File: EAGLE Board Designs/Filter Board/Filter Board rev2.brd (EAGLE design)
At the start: 50.8 x 152.4 mm, 102 parts, among them J4 CONNECTOR-40__, J5 CONNECTOR-40__, U10 MAX7400, U11 MAX7400, U19 MAX7400, U20 MAX7400, U21 MAX7400, U22 MAX7400, U23 MAX7400, U24 MAX7400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

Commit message: fixed drc
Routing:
- net GND: track 59.9 -> 62.7 mm, vias 11 -> 10
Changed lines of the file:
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@@
 <wire x1="44.4956" y1="63.4844" x2="45.45" y2="62.53" width="0.254" layer="16"/>
 <via x="20.574" y="41.402" extent="1-16" drill="0.3556"/>
-<via x="24.13" y="41.402" extent="1-16" drill="0.3556"/>
 <wire x1="19.292" y1="35.052" x2="20.574" y2="35.052" width="0.254" layer="1"/>
 <via x="20.574" y="35.052" extent="1-16" drill="0.3556"/>
@@
 <contactref element="C6" pad="2"/>
 <contactref element="C2" pad="2"/>
-<wire x1="20.574" y1="41.402" x2="24.13" y2="41.402" width="0.254" layer="16"/>
 <wire x1="19.292" y1="41.402" x2="20.574" y2="41.402" width="0.254" layer="1"/>
 <wire x1="19.546" y1="68.326" x2="21.082" y2="68.326" width="0.254" layer="1"/>
@@
 <wire x1="19.292" y1="44.196" x2="19.292" y2="41.402" width="0.254" layer="1"/>
 <wire x1="19.292" y1="35.052" x2="19.292" y2="32.258" width="0.254" layer="1"/>
+<wire x1="20.574" y1="41.402" x2="20.574" y2="35.052" width="0.254" layer="16"/>
 </signal>
 <signal name="LOAD_FL_EXT">
@@
 <contactref element="J4" pad="17"/>
 <contactref element="U7" pad="5"/>
-<wire x1="43.45" y1="105.87" x2="43.386" y2="105.87" width="0.254" layer="1"/>
 <wire x1="43.45" y1="105.87" x2="41.212" y2="103.632" width="0.254" layer="1"/>
 <wire x1="41.212" y1="103.632" x2="29.464" y2="103.632" width="0.254" layer="1"/>
@@
 <signal name="SPN_POT_2">
 <contactref element="J4" pad="25"/>
-<wire x1="43.116" y1="97.536" x2="43.45" y2="97.87" width="0.254" layer="1"/>
 <contactref element="R4" pad="2"/>
 <contactref element="R6" pad="1"/>
@@
 <wire x1="30.734" y1="95.9224" x2="30.834" y2="95.8224" width="0.254" layer="1"/>
 <wire x1="34.798" y1="95.8224" x2="33.02" y2="95.8224" width="0.254" layer="1"/>
-<wire x1="43.45" y1="97.87" x2="41.4024" y2="95.8224" width="0.254" layer="1"/>
-<wire x1="41.4024" y1="95.8224" x2="34.798" y2="95.8224" width="0.254" layer="1"/>
+<wire x1="34.798" y1="95.8224" x2="41.4024" y2="95.8224" width="0.254" layer="1"/>
+<wire x1="41.4024" y1="95.8224" x2="43.45" y2="97.87" width="0.254" layer="1"/>
 </signal>
 <signal name="SPN_POT_3">
@@
 <wire x1="33.02" y1="86.9832" x2="30.834" y2="86.9832" width="0.254" layer="1"/>
 <wire x1="34.798" y1="86.9832" x2="33.02" y2="86.9832" width="0.254" layer="1"/>
-<wire x1="34.798" y1="86.9832" x2="34.886" y2="87.0712" width="0.254" layer="1"/>
 <wire x1="43.45" y1="89.87" x2="43.45" y2="89.844" width="0.254" layer="1"/>
 <wire x1="43.45" y1="89.844" x2="40.5892" y2="86.9832" width="0.254" layer="1"/>
@@
 <contactref element="C2" pad="1"/>
 <wire x1="45.45" y1="40.53" x2="45.068" y2="40.53" width="0.254" layer="1"/>
-<wire x1="44.2764" y1="41.3216" x2="37.4236" y2="41.3216" width="0.254" layer="1"/>
-<wire x1="37.4236" y1="41.3216" x2="37.338" y2="41.236" width="0.254" layer="1"/>
-<wire x1="45.068" y1="40.53" x2="44.2764" y2="41.3216" width="0.254" layer="1"/>
+<wire x1="44.0224" y1="41.5756" x2="37.6776" y2="41.5756" width="0.254" layer="1"/>
+<wire x1="37.6776" y1="41.5756" x2="37.338" y2="41.236" width="0.254" layer="1"/>
+<wire x1="45.068" y1="40.53" x2="44.0224" y2="41.5756" width="0.254" layer="1"/>
 <wire x1="37.338" y1="41.236" x2="34.898" y2="41.236" width="0.254" layer="1"/>
 <wire x1="34.798" y1="41.136" x2="34.898" y2="41.236" width="0.254" layer="1"/>
@@
 <wire x1="5.08" y1="30.492" x2="7.62" y2="30.492" width="0.254" layer="1"/>
 <wire x1="23.876" y1="29.222" x2="26.416" y2="29.222" width="0.254" layer="1"/>
-<wire x1="5.334" y1="40.144" x2="7.62" y2="40.144" width="0.254" layer="1"/>
-<wire x1="7.62" y1="40.144" x2="7.759" y2="40.259" width="0.254" layer="1"/>
-<wire x1="7.759" y1="40.259" x2="10.0965" y2="40.259" width="0.254" layer="1"/>
-<wire x1="5.334" y1="49.034" x2="7.62" y2="49.034" width="0.254" layer="1"/>
-<wire x1="7.62" y1="49.034" x2="7.759" y2="49.149" width="0.254" layer="1"/>
-<wire x1="7.759" y1="49.149" x2="10.0965" y2="49.149" width="0.254" layer="1"/>
 <wire x1="7.62" y1="58.178" x2="5.08" y2="58.178" width="0.254" layer="1"/>
-<wire x1="7.759" y1="58.039" x2="10.0965" y2="58.039" width="0.254" layer="1"/>
 <wire x1="24.13" y1="51.066" x2="26.67" y2="51.066" width="0.254" layer="1"/>
 <wire x1="26.67" y1="51.066" x2="26.555" y2="51.181" width="0.254" layer="1"/>
@@
 <wire x1="9.4735" y1="30.492" x2="10.0965" y2="31.115" width="0.254" layer="1"/>
 <wire x1="24.384" y1="61.734" x2="26.67" y2="61.734" width="0.254" layer="1"/>
-<wire x1="7.759" y1="58.039" x2="7.62" y2="58.178" width="0" layer="19" extent="1-1"/>
+<wire x1="5.334" y1="40.144" x2="7.62" y2="40.144" width="0.254" layer="1"/>
+<wire x1="7.62" y1="40.144" x2="9.9815" y2="40.144" width="0.254" layer="1"/>
+<wire x1="9.9815" y1="40.144" x2="10.0965" y2="40.259" width="0.254" layer="1"/>
+<wire x1="5.334" y1="49.034" x2="7.62" y2="49.034" width="0.254" layer="1"/>
+<wire x1="7.62" y1="49.034" x2="9.9815" y2="49.034" width="0.254" layer="1"/>
+<wire x1="9.9815" y1="49.034" x2="10.0965" y2="49.149" width="0.254" layer="1"/>
+<wire x1="10.0965" y1="58.039" x2="7.759" y2="58.039" width="0.254" layer="1"/>
+<wire x1="7.759" y1="58.039" x2="7.62" y2="58.178" width="0.254" layer="1"/>
 </signal>
 <signal name="CURRENT">

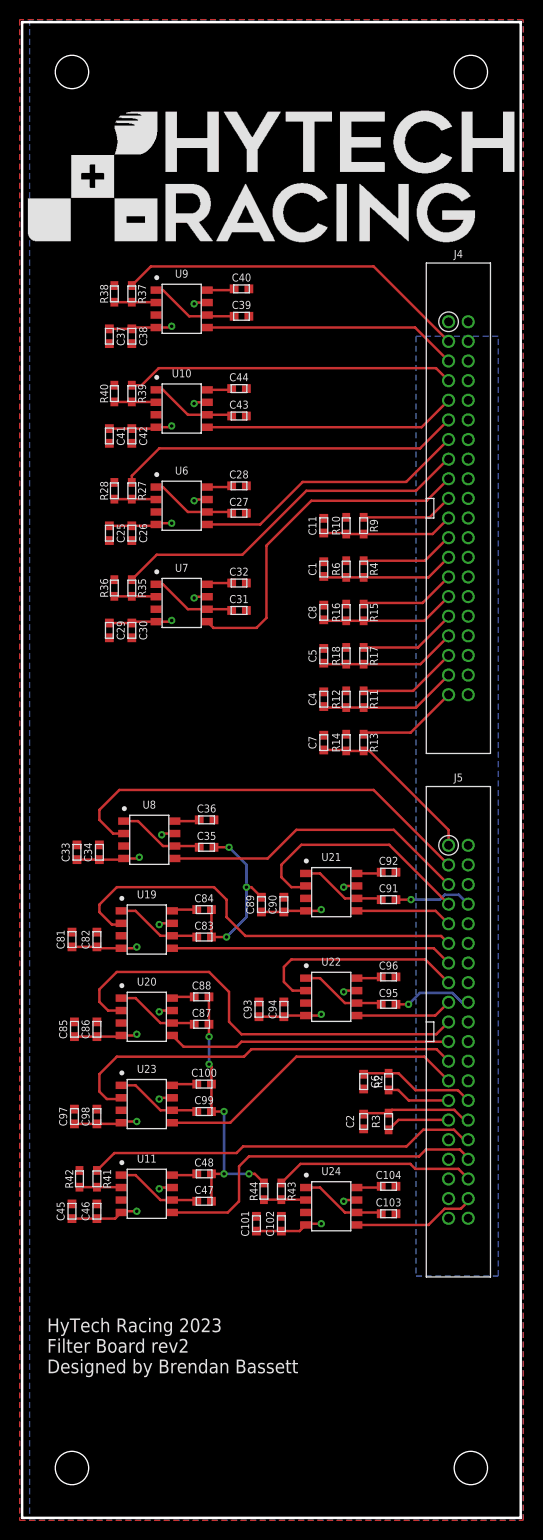
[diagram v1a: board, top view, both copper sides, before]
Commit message: updated passive filters and routing
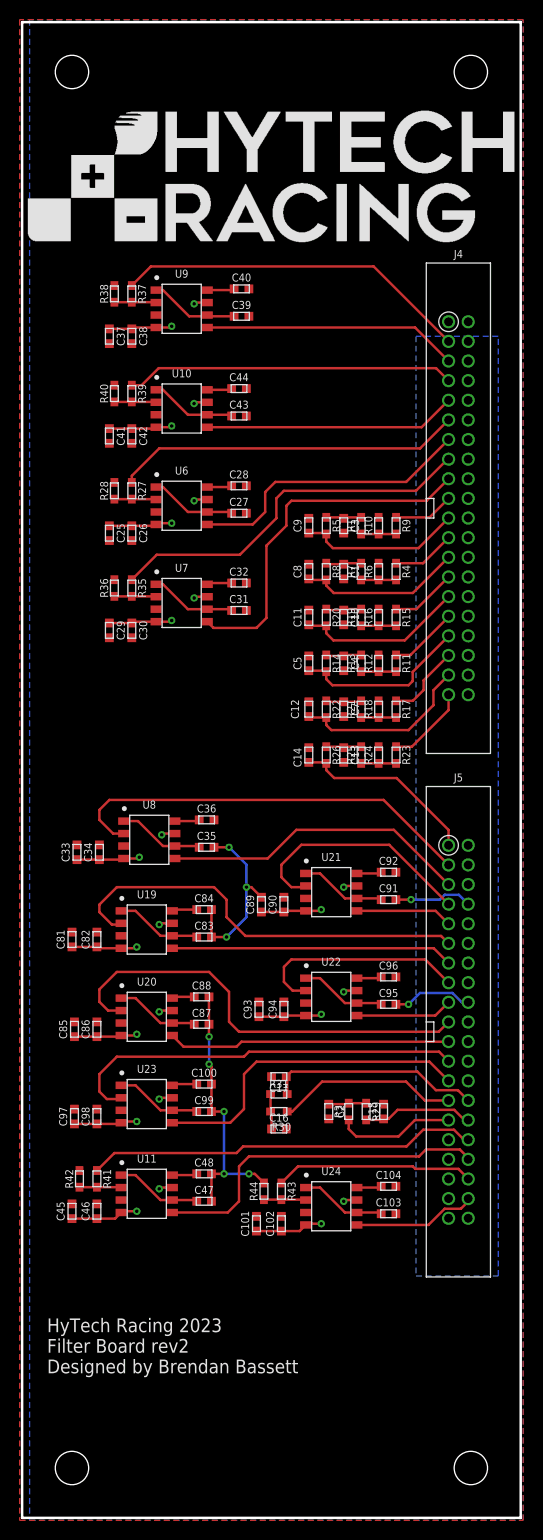
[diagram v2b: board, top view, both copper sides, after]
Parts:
- removed C6: CAPACITOR_0603_25V_1UF, HyTechDevices:0603-CAP
- removed R2: RESISTOR_0603_3.3K, HyTechDevices:0603-RES
- added C10, C12, C13, C14, C15, C16, C17, C3, C9: CAPACITOR_0603_10V_68NF, HyTechDevices:0603-CAP
- added R1, R19, R20, R21, R22, R25, R26, R29, R30, R31, R5, R7, R8: RESISTOR_0603_10K, HyTechDevices:0603-RES
- added R23: RESISTOR_0603_13K, HyTechDevices:0603-RES
- added R24: RESISTOR_0603_3.3K, HyTechDevices:0603-RES
- C1, C11, C2, C4, C5, C7, C8: value CAPACITOR_0603_25V_1UF -> CAPACITOR_0603_10V_68NF
- R13: value RESISTOR_0603_13K -> RESISTOR_0603_10K
- R14, R3: value RESISTOR_0603_3.3K -> RESISTOR_0603_10K
- moved C11 9.47 mm to (29.2, 91.7)
- moved R14 8.33 mm to (31.0, 87.1), turned to 270 degrees
- moved R13 8.08 mm to (34.5, 87.1), turned to 90 degrees
- moved R17 6.36 mm to (38.1, 82.4)
- moved R18 6.36 mm to (36.3, 82.4)
- moved R11 4.93 mm to (38.1, 87.1)
- moved R12 4.93 mm to (36.3, 87.1)
- moved C8 4.44 mm to (29.2, 96.4)
- moved R3 4.19 mm to (33.3, 41.4)
- moved C4 4.18 mm to (32.8, 87.1), turned to 270 degrees
- moved C7 3.96 mm to (32.8, 82.4), turned to 270 degrees
- moved C2 3.70 mm to (31.2, 41.4)
- moved R15 3.34 mm to (38.1, 91.7)
- moved R16 3.34 mm to (36.3, 91.7)
- moved R4 3.31 mm to (38.1, 96.4)
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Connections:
- new net N$10: R11.2, R12.1, R13.1
- new net N$11: C7.1, R21.2, R22.1
- new net N$12: R17.2, R18.1, R21.1
- new net N$25: C13.1, R25.2, R26.1
- new net N$26: R23.2, R24.1, R25.1
- new net N$27: C2.1, R29.1, R3.2
- new net N$28: C16.1, R30.2, R31.1
- new net N$3: C3.1, R1.2, R5.1
- new net N$4: C1.1, R7.2, R8.1
- new net N$5: R1.1, R10.1, R9.2
- new net N$6: R4.2, R6.1, R7.1
- new net N$7: C10.1, R19.2, R20.1
- new net N$8: R15.2, R16.1, R19.1
- new net N$9: C4.1, R13.2, R14.1
- net BRAKE_PRESSURE_F: now also C17.1, R31.2; no longer C6.1, R2.2
- net BRAKE_PRESSURE_F_EXT: now also R30.1; no longer R2.1
- net BRAKE_PRESSURE_R: now also C15.1, R29.2; no longer C2.1, R3.2
- net GND: now also C10.2, C12.2, C13.2, C14.2, C15.2, C16.2, C17.2, C3.2, C9.2, R24.2; no longer C6.2, R14.2
- net SPN_POT_1: now also C9.1, R5.2; no longer C11.1, R10.1, R9.2
- net SPN_POT_2: now also C8.1, R8.2; no longer C1.1, R4.2, R6.1
- net SPN_POT_3: now also C11.1, R20.2; no longer C8.1, R15.2, R16.1
- net SPN_POT_4: now also R14.2; no longer R17.2, R18.1
- net SPN_POT_4_EXT: now also R11.1; no longer R17.1
- net SPN_POT_5: now also C12.1, R22.2; no longer C4.1, R11.2, R12.1
- net SPN_POT_5_EXT: now also R17.1; no longer R11.1
- net SPN_POT_6: now also C14.1, R26.2; no longer C7.1, R13.2, R14.1
- net SPN_POT_6_EXT: now also R23.1; no longer R13.1
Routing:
- net BRAKE_PRESSURE_F_EXT: track 6.56 -> 18.5 mm
- net BRAKE_PRESSURE_F: track 11.8 -> 21.8 mm
- net BRAKE_PRESSURE_R_EXT: track 6.54 -> 12.1 mm
- net SPN_POT_5: track 14.1 -> 18.5 mm
- net SPN_POT_4: track 14.0 -> 17.9 mm
- net N$27: track 0.00 -> 3.85 mm
- net N$11: track 0.00 -> 3.64 mm
- net N$7: track 0.00 -> 3.64 mm
- net N$9: track 0.00 -> 3.64 mm
- net N$4: track 0.00 -> 3.64 mm
- net N$3: track 0.00 -> 3.64 mm
- net N$25: track 0.00 -> 3.64 mm
- net N$28: track 0.00 -> 3.60 mm
- net N$8: track 0.00 -> 3.56 mm
- net N$6: track 0.00 -> 3.56 mm
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
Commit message: labels for all passive components visible
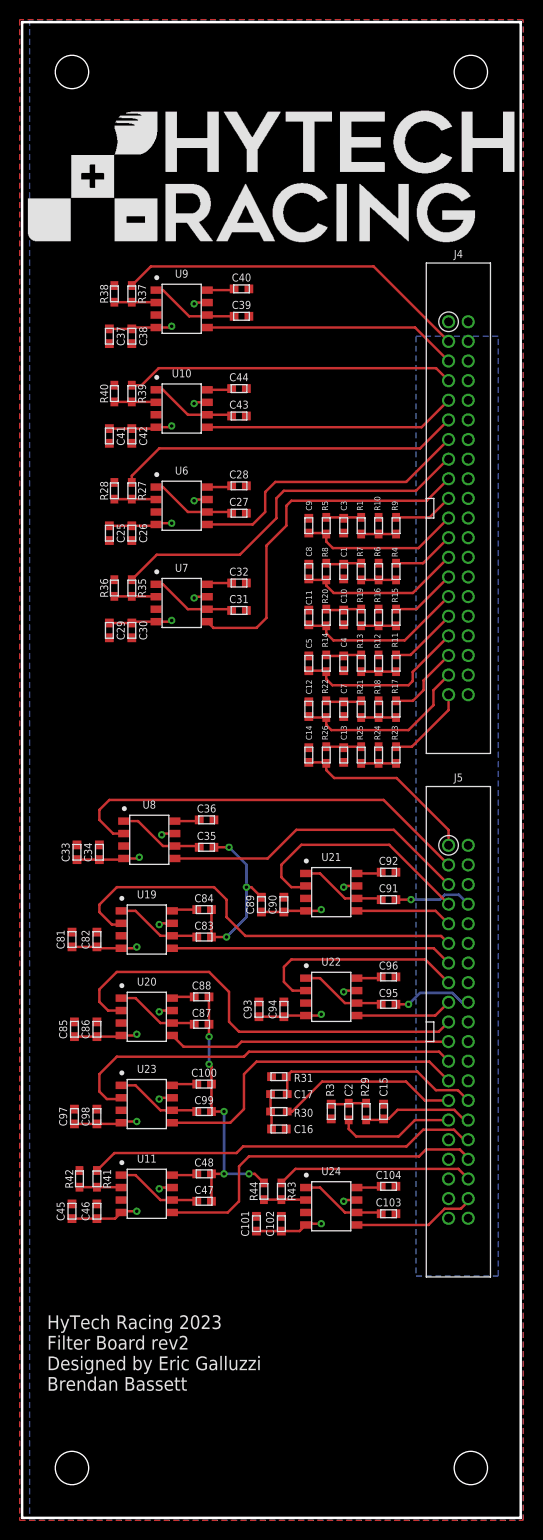
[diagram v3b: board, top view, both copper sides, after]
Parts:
- moved C2 0.25 mm to (31.5, 41.4)
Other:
- board text added: "HyTech Racing 2023 Filter Board rev2 Designed by Eric Galluzzi Brendan Bassett"
- board text removed: "HyTech Racing 2023 Filter Board rev2 Designed by Brendan Bassett"
